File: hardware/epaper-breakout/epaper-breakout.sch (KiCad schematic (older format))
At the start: 90 parts, among them J1 XF2M-3315-1A, J2 C10418, J3 Conn_02x06_Counter_Clockwise, J4 ED060SC4, J5 Conn_01x01_Male, J6 Conn_01x01_Male, Q1 AO3401A, Q2 AO3401A, Q3 MMBT3904, Q4 MMBT3904, Q5 AO3401A, Q6 MMBT3904, U1 MCP1700-3302E_SOT23, U10 ED060SC7, U11 TP4056, U12 CH340C, U2 LT1945, U3 LT1945, U4 XC6206PxxxMR, U5 ESP32-WROVER, U6 ED060XC5, U7 LM358, U8 74HC4094-normal, U9 MCP9700AT-ETT

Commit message: minor change in V5
exchange L1 <-> U2 position
change usb connector footprint
change U6 footprint
chang RV1 footprint
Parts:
- J2: footprint epaper-breakout:USB_Micro-B_A01SB141B1-067 -> epaper-breakout:JLC_MICRO-USB-SMD_A4A0507-E-01-R
- RV1: footprint epaper-breakout:EVM3ESX50B25 -> epaper-breakout:JLC_RES-ADJ-TH_3362P
- U6: footprint epaper-breakout:X05A20H34G -> epaper-breakout:JLC_FFC-SMD_34P-P0.50_FH34SRJ-34S-0.5SH
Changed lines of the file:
@@
 F 0 "RV1" H 4131 10296 50  0000 R CNN
 F 1 "200k" H 4131 10205 50  0000 R CNN
-F 2 "epaper-breakout:EVM3ESX50B25" H 4200 10250 50  0001 C CNN
+F 2 "epaper-breakout:JLC_RES-ADJ-TH_3362P" H 4200 10250 50  0001 C CNN
 F 3 "https://lcsc.com/product-detail/Variable-Resistors_PANASONIC-EVM3ESX50B25_C11958.html" H 4200 10250 50  0001 C CNN
 F 4 "C11958" H 4200 10250 50  0001 C CNN "LCSC"
@@
 F 0 "J2" H 857 10517 50  0000 C CNN
 F 1 "C10418" H 857 10426 50  0000 C CNN
-F 2 "epaper-breakout:USB_Micro-B_A01SB141B1-067" H 950 10000 50  0001 C CNN
+F 2 "epaper-breakout:JLC_MICRO-USB-SMD_A4A0507-E-01-R" H 950 10000 50  0001 C CNN
 F 3 "https://lcsc.com/product-detail/USB-Connectors_Jing-Extension-of-the-Electronic-Co-Jing-Extension-of-the-Electronic-Co-MICRO-USB-5S-B-Type-horns-High-temperature_C10418.html" H 950 10000 50  0001 C CNN
 F 4 "C10418" H 800 10050 50  0001 C CNN "LCSC"
@@
 F 0 "U6" H 13478 7796 50  0000 L CNN
 F 1 "ED060XC5" H 13478 7705 50  0000 L CNN
-F 2 "epaper-breakout:X05A20H34G" H 12950 9600 50  0001 C CNN
+F 2 "epaper-breakout:JLC_FFC-SMD_34P-P0.50_FH34SRJ-34S-0.5SH" H 12950 9600 50  0001 C CNN
 F 3 "http://www.universaldisplay.asia/wp-content/uploads/2012/10/ED060XC5.pdf, https://datasheet.lcsc.com/szlcsc/2005221833_XKB-Connectivity-X05A20H34G_C528053.pdf" H 12950 9600 50  0001 C CNN
 	1    12900 7750

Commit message: New version board base on V5
Add Touch screen connector
Add RTC
Add Buzzer
Change USB-MicroB to USB-C
Change Battery connector
Change footprint
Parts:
- removed J1: XF2M-3315-1A, epaper-breakout:CONN_ED097OC4, symbol epd_breakout:XF2M-3315-1A
- removed J4: ED060SC4, epaper-breakout:HRS_FH26W-39S-0.3SHW(60), symbol ed060sc4:ED060SC4
- removed J5, J6: Conn_01x01_Male, Connector_PinHeader_2.54mm:PinHeader_1x01_P2.54mm_Vertical, symbol Connector:Conn_01x01_Male
- removed U10: ED060SC7, epaper-breakout:AXT334124, symbol epd_breakout:ED060SC7
- added BT1: Battery_Cell, epaper-breakout:JLC_BAT-SMD_MY-1220-03, symbol Device:Battery_Cell
- added BZ1: Buzzer, epaper-breakout:JLC_BUZ-SMD_4P-L8.5-W8.5_FUET-8530-05, symbol Device:Buzzer
- added C24, C25: 22pF, Capacitor_SMD:C_0603_1608Metric, symbol Device:C
- added C26, C27: 10uF, Capacitor_SMD:C_0603_1608Metric, symbol Device:C
- added D11, D12, D13: 1N5817, Diode_SMD:D_SOD-123, symbol Diode:1N5817
- added H4, H5, H6: MountingHole, MountingHole:MountingHole_4mm, symbol Mechanical:MountingHole
- added Q7: 2N7002, Package_TO_SOT_SMD:SOT-23, symbol Transistor_FET:2N7002
- added R23, R24: 5.1K, Resistor_SMD:R_0805_2012Metric, symbol Device:R
- added R25: 33, Resistor_SMD:R_0603_1608Metric, symbol Device:R
- added R26: 1k, Resistor_SMD:R_0805_2012Metric, symbol Device:R
- added R27: 100k, Resistor_SMD:R_0805_2012Metric, symbol Device:R
- added SW1: SW_DIP_x01, epaper-breakout:JLC_SW-SMD_MK-12C02-G025, symbol epd_breakout:SW_DIP_x01
- added TP2: TestPoint_Probe, TestPoint:TestPoint_Pad_D1.0mm, symbol Connector:TestPoint_Probe
- added U10: FPC-TOUCH, epaper-breakout:JLC_FFC-SMD_6P-P0.50_FH34SRJ-6S-0.5SH, symbol epd_breakout:FPC-TOUCH
- added U13: CONN-Battery, epaper-breakout:JLC_CONN-SMD_A1254WR-S-2P, symbol epd_breakout:CONN-Battery
- added U14: PCF8563T, Package_SO:SOIC-8_3.9x4.9mm_P1.27mm, symbol Timer_RTC:PCF8563T
- added Y1: Crystal, epaper-breakout:JLC_CRYSTAL-SMD_L7.0-W3.2-LS7.5, symbol Device:Crystal
- H3: footprint MountingHole:MountingHole_2.2mm_M2 -> MountingHole:MountingHole_4mm
- J2: value C10418 -> USB_C_16P; footprint epaper-breakout:JLC_MICRO-USB-SMD_A4A0507-E-01-R -> epaper-breakout:JLC_USB-C-SMD_KH-TYPE-C-16P; symbol epd_breakout:C10418 -> Connector:USB_C_Receptacle_USB2.0; LCSC C10418 -> C709357
- L1, L2, L3, L4: footprint Inductor_SMD:L_6.3x6.3_H3 -> epaper-breakout:JLC_IND-SMD_L4.0-W4.0_SMNR4020; LCSC C206321 -> C135264
- RV1: footprint epaper-breakout:JLC_RES-ADJ-TH_3362P -> epaper-breakout:JLC_RES-ADJ-SMD_VG039NCH; LCSC C11958 -> C128551
- U11: symbol tp4056:TP4056 -> epaper-breakout-rescue:TP4056-tp4056
- U6: footprint epaper-breakout:JLC_FFC-SMD_34P-P0.50_FH34SRJ-34S-0.5SH -> epaper-breakout:X05A20H34G
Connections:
- net +3.3V: now also C27.2, D11.2 (A), R25.2, U10.1 (VDD)
- net BAT+: now also U13.1
- net GND: now also J2.A1 (GND), J2.A12 (GND), J2.B1 (GND), J2.B12 (GND), J2.S1 (SHIELD), BT1.2 (-), C24.2, C25.2, C26.1, C27.1, Q7.2 (S), R23.2, R24.2, R27.1, SW1.4 (Shield), SW1.5 (Shield), SW1.6 (Shield), SW1.7 (Shield), U10.2 (GND), U13.2, U13.3 (S), U13.4 (S), U14.4 (VSS); no longer J2.5 (GND), J2.6 (Shield)
- net VBUS: now also J2.A4 (VBUS), J2.A9 (VBUS), J2.B4 (VBUS), J2.B9 (VBUS); no longer J2.1 (VBUS)
- net VIN: now also SW1.1, SW1.2; no longer C2.2, U1.3 (VI)
- net USB_D-: now reaches U12.6 (UD-)
- net USB_D-: now also J2.A7 (D-), J2.B7 (D-); no longer J2.2 (D-)
- net USB_D+: now reaches U12.5 (UD+)
- net USB_D+: now also J2.A6 (D+), J2.B6 (D+); no longer J2.3 (D+)
- net TCH_INT: now reaches U5.17 (SD2_IO9)
- net TCH_INT: now also U10.5 (INT)
- net TCH_RST: now reaches U5.18 (SD3_IO10)
- net TCH_RST: now also U10.6 (RST)
- net TCH_SDA: now reaches U5.21 (SD0_IO7)
- net TCH_SDA: now also U10.4 (SDA), U14.5 (SDA)
- net TCH_SCL: now reaches U5.22 (SD1_IO8)
- net TCH_SCL: now also U10.3 (SCL), U14.6 (SCL)
- net BUZZER: now reaches U5.27 (IO16)
- net BUZZER: now also R26.2
- new net: C2.2, SW1.3, U1.3 (VI)
- new net: J2.A5 (CC1), R23.1
- new net: J2.B5 (CC2), R24.1
- new net: C24.1, C25.1, U14.2 (OSCO), Y1.2
- new net: BZ1.1 (-), D13.1 (K), R25.1
- new net: BZ1.2 (+), D13.2 (A), Q7.3 (D)
- new net: Q7.1 (G), R26.1, R27.2
- new net: TP2.1, U14.7 (CLKO)
- new net: U14.1 (OSCI), Y1.1
- new net: C26.2, D11.1 (K), D12.1 (K), U14.8 (VDD)
- new net: BT1.1 (+), D12.2 (A)
- no-connect marks 28 -> 15
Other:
- moved on the sheet: C13, C14, C16, C2, C3, H1, H2, H3, R14, RV1, TP1, U1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

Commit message: change outline
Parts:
- removed H3, H4: MountingHole, MountingHole:MountingHole_4mm, symbol Mechanical:MountingHole
- renumbered C8 to C10, C9 to C12, C19 to C13, C12 to C14, C20 to C15, C21 to C16, C15 to C17, C17 to C18, C18 to C19, C6 to C2, C2 to C20, C24 to C21, C25 to C22, C22 to C23, C3 to C24, C26 to C25, C27 to C26, C23 to C27, C13 to C3, C7 to C5, C5 to C6, C10 to C7, C14 to C8, C16 to C9, D9 to D10, D4 to D2, D2 to D3, D5 to D4, D3 to D5, D10 to D8, D8 to D9, H5 to H3, H6 to H4, J2 to J1, J3 to J2, Q3 to Q2, Q4 to Q3, Q6 to Q4, Q7 to Q5, Q2 to Q6, Q5 to Q7, R23 to R1, R19 to R10, R14 to R11, R10 to R12, R2 to R13, R3 to R14, R8 to R15, R9 to R16, R13 to R17, R1 to R18, R11 to R19, R24 to R2, R15 to R20, R25 to R23, R12 to R24, R26 to R25, R27 to R26, R20 to R27, R4 to R3, R5 to R4, R16 to R5, R17 to R6, R6 to R7, R7 to R8, R18 to R9, U2 to U1, U5 to U10, U14 to U11, U9 to U12, U6 to U13, U10 to U14, U3 to U2, U4 to U3, U12 to U4, U8 to U5, U7 to U6, U13 to U7, U11 to U8, U1 to U9

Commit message: fabrication update
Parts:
- R23: LCSC C2838960 -> C72812
- SW1: Field4 C778186 -> (none); LCSC (none) -> C778186
- U1, U2: LCSC (none) -> C665600
- U11: LCSC (none) -> C7440
- U13: LCSC (none) -> C528053
- U7: LCSC (none) -> C272975
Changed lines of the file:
@@
 F 2 "Package_SO:MSOP-10_3x3mm_P0.5mm" H 2100 1550 50  0001 L CNN
 F 3 "https://www.analog.com/media/en/technical-documentation/data-sheets/1945fa.pdf" H 2150 1800 50  0001 C CNN
+F 4 "C665600" H 2050 1800 50  0001 C CNN "LCSC"
 	1    2050 1800
 	1    0    0    -1
@@
 F 2 "Package_SO:MSOP-10_3x3mm_P0.5mm" H 2100 5600 50  0001 L CNN
 F 3 "https://www.analog.com/media/en/technical-documentation/data-sheets/1945fa.pdf" H 2150 5850 50  0001 C CNN
+F 4 "C665600" H 2050 5850 50  0001 C CNN "LCSC"
 	1    2050 5850
 	1    0    0    -1
@@
 F 2 "epaper-breakout:X05A20H34G" H 15000 9750 50  0001 C CNN
 F 3 "http://www.universaldisplay.asia/wp-content/uploads/2012/10/ED060XC5.pdf, https://datasheet.lcsc.com/szlcsc/2005221833_XKB-Connectivity-X05A20H34G_C528053.pdf" H 15000 9750 50  0001 C CNN
+F 4 "C528053" H 14950 7900 50  0001 C CNN "LCSC"
 	1    14950 7900
 	1    0    0    -1
@@
 F 2 "epaper-breakout:JLC_SW-SMD_MK-12C02-G025" H 7800 10700 50  0001 C CNN
 F 3 "https://item.szlcsc.com/826787.html" H 7800 10700 50  0001 C CNN
-F 4 " C778186" V 7800 10700 50  0001 C CNN "Field4"
+F 4 " C778186" V 7800 10700 50  0001 C CNN "LCSC"
 	1    7800 10700
 	0    -1   1    0
@@
 F 2 "epaper-breakout:JLC_CONN-SMD_A1254WR-S-2P" H 6828 6709 50  0000 L CNN
 F 3 "https://item.szlcsc.com/261346.html" H 6400 6550 50  0001 C CNN
+F 4 " C272975" H 6600 6800 50  0001 C CNN "LCSC"
 	1    6600 6800
 	1    0    0    -1
@@
 F 2 "Package_SO:SOIC-8_3.9x4.9mm_P1.27mm" H 9450 8800 50  0001 C CNN
 F 3 "https://assets.nexperia.com/documents/data-sheet/PCF8563.pdf" H 9450 8800 50  0001 C CNN
-F 4 "~" H 9450 8800 50  0001 C CNN "LCSC"
+F 4 "C7440" H 9450 8800 50  0001 C CNN "LCSC"
 	1    9450 8800
 	1    0    0    -1
@@
 F 1 "33" H 11620 8055 50  0000 L CNN
 F 2 "Resistor_SMD:R_0603_1608Metric" V 11480 8100 50  0001 C CNN
-F 3 "https://item.szlcsc.com/3014656.html" H 11550 8100 50  0001 C CNN
-F 4 " C2838960" H 11550 8100 50  0001 C CNN "LCSC"
+F 3 "https://item.szlcsc.com/73924.html" H 11550 8100 50  0001 C CNN
+F 4 "C72812" H 11550 8100 50  0001 C CNN "LCSC"
 	1    11550 8100
 	0    1    1    0

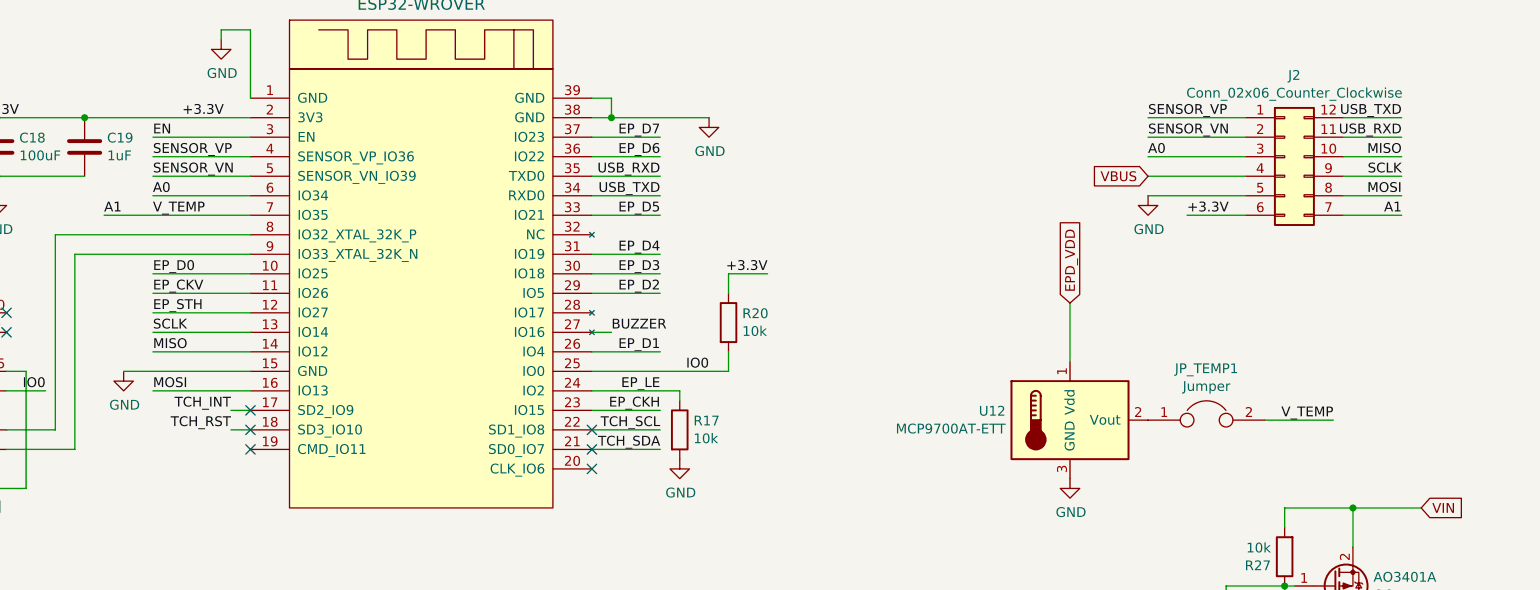
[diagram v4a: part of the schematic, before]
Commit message: change i2c bus pin
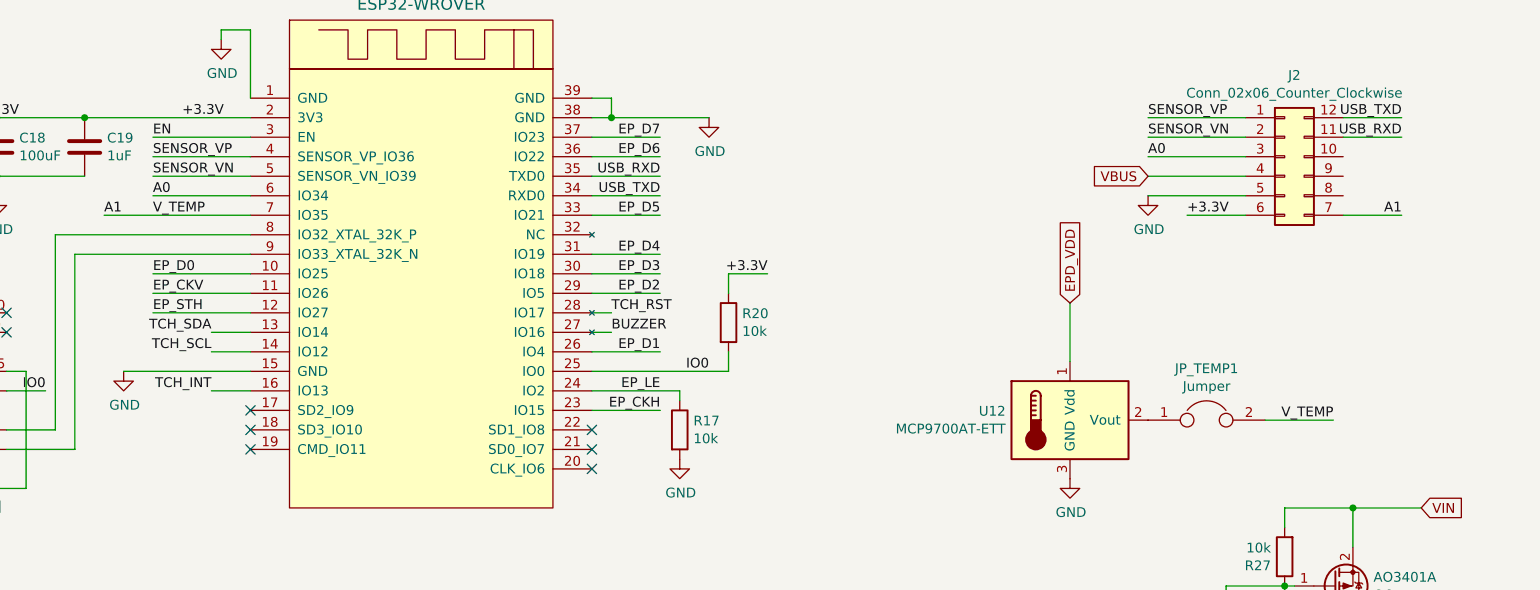
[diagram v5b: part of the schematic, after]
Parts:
- R13: LCSC C17407 -> C149504
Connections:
- net TCH_INT: now also U10.16 (IO13); no longer U10.17 (SD2_IO9)
- net TCH_RST: now also U10.28 (IO17); no longer U10.18 (SD3_IO10)
- net TCH_SCL: now also U10.14 (IO12); no longer U10.22 (SD1_IO8)
- net TCH_SDA: now also U10.13 (IO14); no longer U10.21 (SD0_IO7)
- net MISO: no longer names the net of J2.10 (Pin_10)
- net MISO: no longer U10.14 (IO12)
- net MOSI: no longer names the net of J2.8 (Pin_8)
- net MOSI: no longer U10.16 (IO13)
- net SCLK: no longer names the net of J2.9 (Pin_9)
- net SCLK: no longer U10.13 (IO14)
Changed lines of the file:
@@
 Wire Wire Line
 	5450 3100 5950 3100
-Text Label 7500 2600 0    50   ~ 0
-MISO
-Text Label 7500 2500 0    50   ~ 0
-SCLK
-Text Label 7500 2800 0    50   ~ 0
-MOSI
 $Comp
 L esp32-wrover:ESP32-WROVER U10
@@
 Text Label 10100 2800 2    50   ~ 0
 EP_LE
-Wire Wire Line
-	8000 2800 7500 2800
 $Comp
 L power:GND #PWR035
@@
 Wire Wire Line
 	5900 1400 6000 1400
-Wire Wire Line
-	7500 2600 8000 2600
-Wire Wire Line
-	8000 2500 7500 2500
-Text Label 13900 1600 2    50   ~ 0
-MISO
-Text Label 13900 1700 2    50   ~ 0
-SCLK
-Text Label 13900 1800 2    50   ~ 0
-MOSI
 Text Label 13900 1900 2    50   ~ 0
 A1
@@
 Wire Wire Line
 	12600 1500 13100 1500
-Wire Wire Line
-	13900 1600 13600 1600
-Wire Wire Line
-	13900 1700 13600 1700
-Wire Wire Line
-	13900 1800 13600 1800
 Wire Wire Line
 	13900 1900 13600 1900
@@
 F 2 "Resistor_SMD:R_0805_2012Metric" V 6530 5900 50  0001 C CNN
 F 3 "~" H 6600 5900 50  0001 C CNN
-F 4 "C17407" V 6600 5900 50  0001 C CNN "LCSC"
+F 4 " C149504" V 6600 5900 50  0001 C CNN "LCSC"
 	1    6600 5900
 	0    1    1    0
@@
 	1    0    0    -1
 $EndComp
-Text Label 10100 3100 2    50   ~ 0
+Text Label 7800 2500 2    50   ~ 0
 TCH_SDA
-Text Label 10100 3000 2    50   ~ 0
+Text Label 7800 2600 2    50   ~ 0
 TCH_SCL
-Wire Wire Line
-	9750 3100 10100 3100
-Wire Wire Line
-	10100 3000 9750 3000
 Text Label 14650 5450 2    50   ~ 0
 TCH_SCL
@@
 Text Label 14600 5750 2    50   ~ 0
 TCH_RST
-Text Label 7900 2900 2    50   ~ 0
+Text Label 7800 2800 2    50   ~ 0
 TCH_INT
-Text Label 7900 3000 2    50   ~ 0
+Text Label 9850 2400 0    50   ~ 0
 TCH_RST
-Wire Wire Line
-	7900 2900 8000 2900
-Wire Wire Line
-	7900 3000 8000 3000
 Wire Wire Line
 	14600 5550 14900 5550
@@
 Wire Wire Line
 	11250 8550 11250 8600
+Wire Wire Line
+	8000 2500 7800 2500
+Wire Wire Line
+	8000 2600 7800 2600
+Wire Wire Line
+	8000 2800 7800 2800
+Wire Wire Line
+	9750 2400 9850 2400
 $EndSCHEMATC
